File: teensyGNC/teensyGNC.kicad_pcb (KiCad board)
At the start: 4 copper layers, 57.5 x 129.5 mm, 32 parts, among them J1 5V_In_JST_XH, J10 TO_92_1_JST_PH, J11 TO_92_2_JST_PH, J12 TO_92_3_JST_PH, J13 TO_92_4_JST_PH, J2 ESC_1_PWM_1x03, J3 ESC_2_PWM_1x03, J4 Servo_1_PWM_1x03, J5 Servo_2_PWM_1x03, J6 7V4_In_XT30M, J7 I2C_INA_BM_JST_GH, J8 MTF_01P_JST_SH, J9 LC29H_Molex_4P, U1 LVL_Shift, U2 E28-2G4T20SX, U3 4754, U4 AP2112K-3.3, U5 DPS310, U6 Teensy4.1

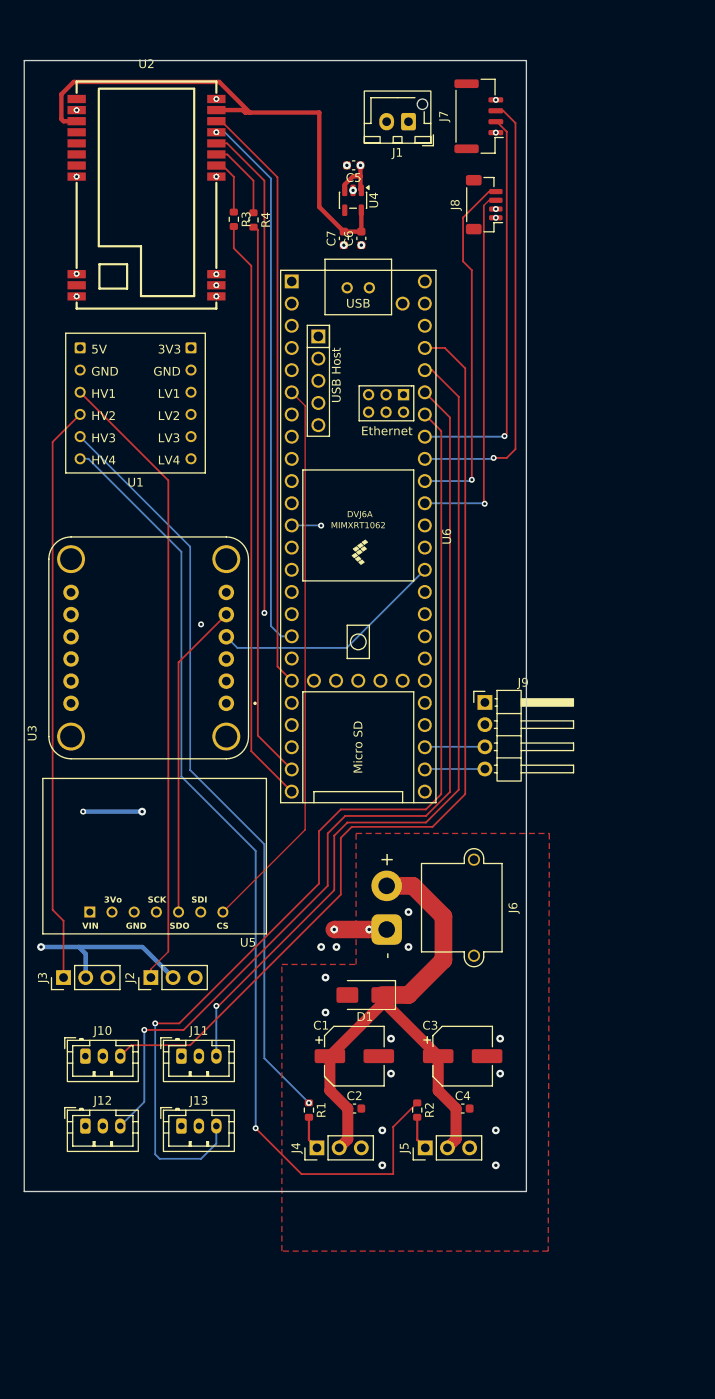
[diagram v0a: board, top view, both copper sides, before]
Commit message: More amendments
- Added mounting holes
- Removed splits in the ground plane by removing all in1.cu plane traces
- Added pull up/down resistors (check values)
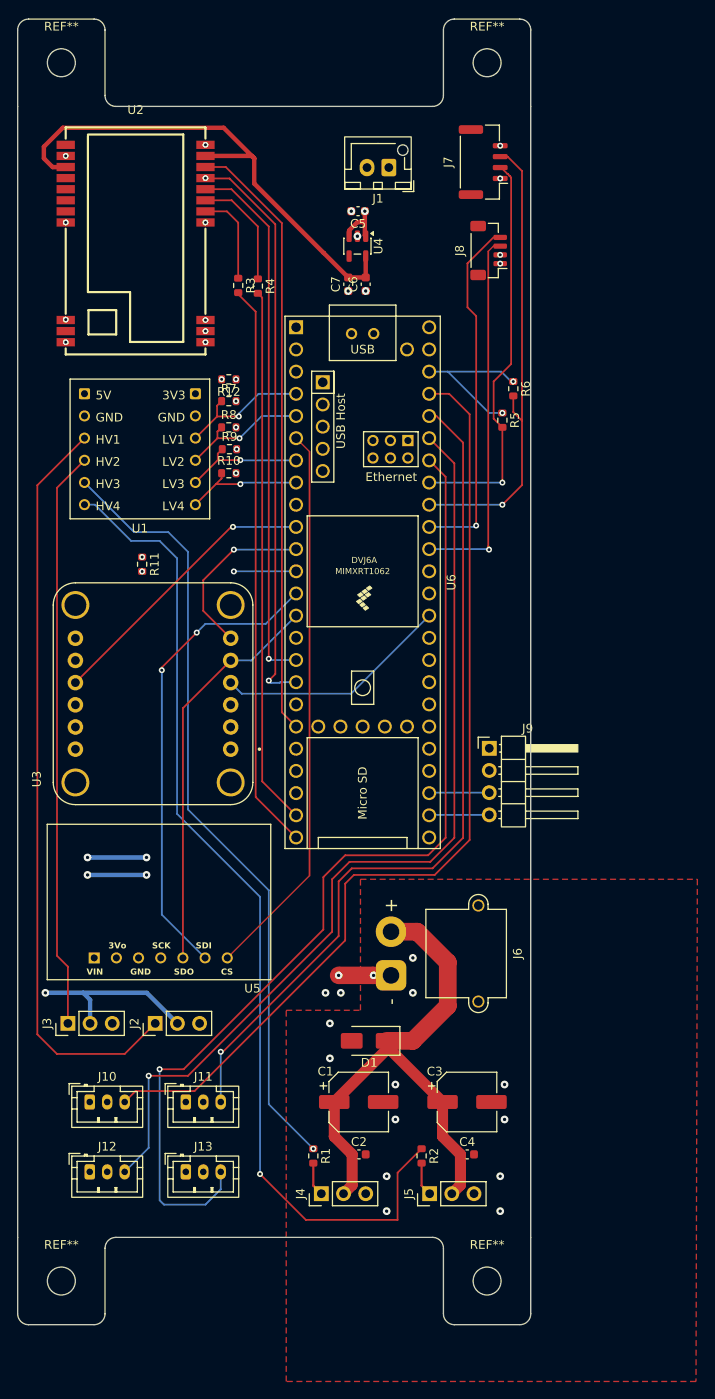
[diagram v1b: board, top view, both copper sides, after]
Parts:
- added R10: 10kΩ, Resistor_SMD:R_0603_1608Metric, F.Cu at (95.4, 78.8)
- added R11: 10kΩ, Resistor_SMD:R_0603_1608Metric, F.Cu at (85.5, 89.2)
- added R12: 10kΩ, Resistor_SMD:R_0603_1608Metric, F.Cu at (95.4, 68.0)
- added R5: 2.2kΩ, Resistor_SMD:R_0603_1608Metric, F.Cu at (126.8, 72.7)
- added R6: 2.2kΩ, Resistor_SMD:R_0603_1608Metric, F.Cu at (128.0, 69.1)
- added R7: 10kΩ, Resistor_SMD:R_0603_1608Metric, F.Cu at (95.4, 70.5)
- added R8: 10kΩ, Resistor_SMD:R_0603_1608Metric, F.Cu at (95.4, 73.5)
- added R9: 10kΩ, Resistor_SMD:R_0603_1608Metric, F.Cu at (95.5, 76.0)
- added REF**: MountingHole_3.2mm_M3, MountingHole:MountingHole_3.2mm_M3, F.Cu at (125.0, 31.8)
- added REF**: MountingHole_3.2mm_M3, MountingHole:MountingHole_3.2mm_M3, F.Cu at (125.0, 171.2)
- added REF**: MountingHole_3.2mm_M3, MountingHole:MountingHole_3.2mm_M3, F.Cu at (76.2, 31.8)
- added REF**: MountingHole_3.2mm_M3, MountingHole:MountingHole_3.2mm_M3, F.Cu at (76.2, 171.2)
- moved R3 7.59 mm to (96.5, 57.2)
- moved R4 7.59 mm to (98.8, 57.3)
- moved J1 5.71 mm to (113.8, 43.8)
- moved U2 5.40 mm to (84.8, 52.5)
- moved C1 5.27 mm to (110.3, 150.8)
- moved C2 5.27 mm to (110.3, 156.8)
- moved C3 5.27 mm to (122.7, 150.8)
- moved C4 5.27 mm to (122.7, 156.8)
- moved C5 5.27 mm to (110.2, 48.8)
- moved C6 5.27 mm to (111.1, 57.1)
- moved C7 5.27 mm to (109.1, 57.1)
- moved D1 5.27 mm to (111.5, 143.8)
- moved J10 5.27 mm to (79.5, 150.8)
- moved J11 5.27 mm to (90.5, 150.8)
- moved J12 5.27 mm to (79.5, 158.8)
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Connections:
- R3 pad 1: Net-(U2-M0) -> GND
- R3 pad 2: Net-(U6-32_OUT1B) -> Net-(U2-M0)
- R4 pad 1: Net-(U2-M1) -> GND
- R4 pad 2: Net-(U6-31_CTX3) -> Net-(U2-M1)
- U6 pad 2: /SPI.CS_BNO -> unconnected-(U6-0_RX1_CRX2_CS1-Pad2)
- U6 pad 23: Net-(U6-31_CTX3) -> Net-(U2-M1)
- U6 pad 24: Net-(U6-32_OUT1B) -> Net-(U2-M0)
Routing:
- net Net-(U2-M0): track 7.15 -> 76.4 mm
- net Net-(U6-32_OUT1B): track 67.5 -> 0.00 mm
- net Net-(U2-M1): track 9.74 -> 75.4 mm
- net Net-(U6-31_CTX3): track 64.0 -> 0.00 mm
- net /SPI.CS_BNO: track 70.8 -> 28.5 mm, vias 1 -> 2
- net +3V3: track 181.1 -> 209.4 mm, vias 2 -> 8
- net /SPI.DI: track 80.2 -> 64.5 mm, vias 1 -> 2
- net Net-(J2-Pin_1): track 72.0 -> 86.4 mm
- net /SPI.CS_DPS: track 64.0 -> 73.7 mm, vias 0 -> 1
- net /SPI.INT: track 13.3 -> 20.1 mm, vias 0 -> 1
- net +5V: track 237.1 -> 243.5 mm
- net Net-(U2-TXD): track 63.1 -> 66.6 mm, vias 1 -> 2
- net Net-(J7-Pin_3): track 51.0 -> 54.0 mm
- net Net-(U2-AUX): track 68.0 -> 70.3 mm
- net Net-(R1-Pad1): track 87.1 -> 89.4 mm
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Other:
- board size 57.5 x 129.5 mm -> 58.8 x 149.5 mm

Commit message: Moved LC29H onboard and to the top of the board
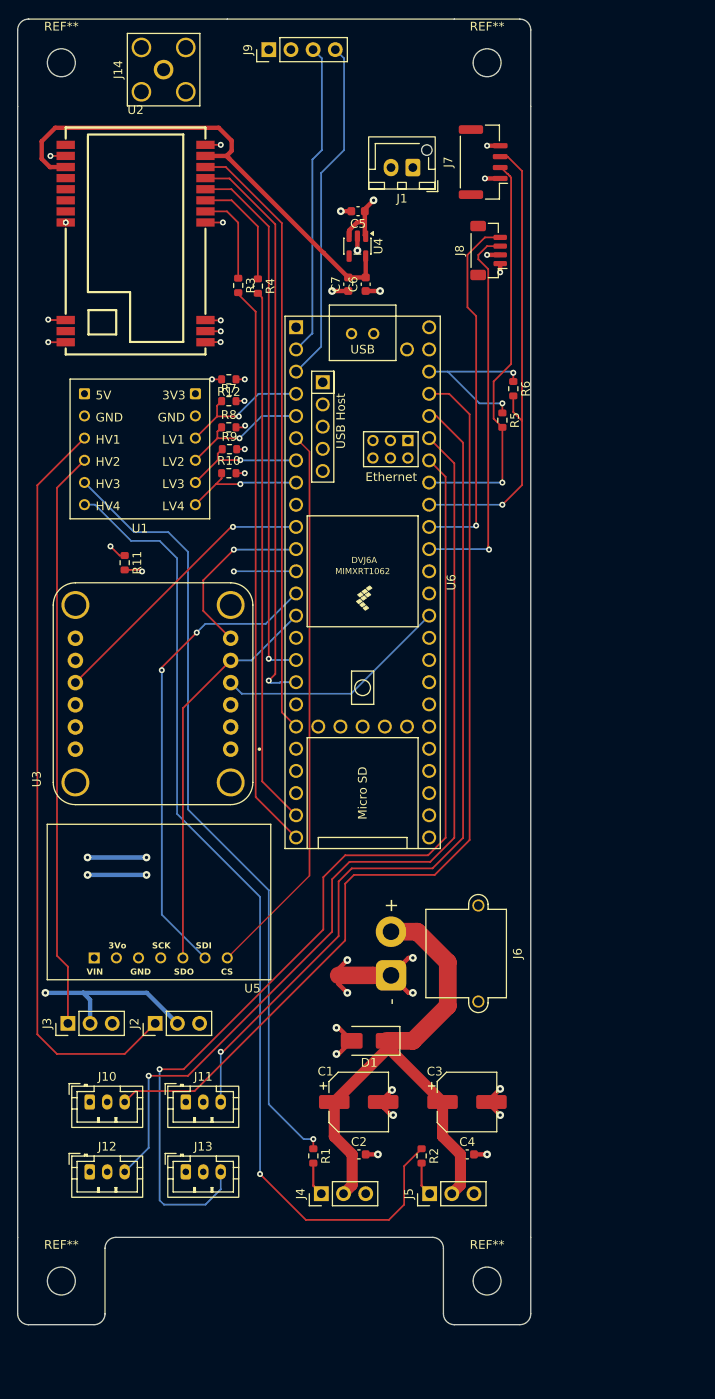
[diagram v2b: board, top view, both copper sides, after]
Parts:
- added J14: Conn_Coaxial, Connector_Coaxial:SMA_Amphenol_132203-12_Horizontal, F.Cu at (88.0, 32.5)
- J9: value LC29H_Molex_4P -> LC29H_1x04; footprint Connector_PinHeader_2.54mm:PinHeader_1x04_P2.54mm_Horizontal -> Connector_PinHeader_2.54mm:PinHeader_1x04_P2.54mm_Vertical
- moved J9 83.9 mm to (100.0, 30.2), turned to 90 degrees
- moved J1 2.75 mm to (116.5, 43.8)
- moved R11 2.01 mm to (83.5, 89.0)
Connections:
- U6 pad 2: unconnected-(U6-0_RX1_CRX2_CS1-Pad2) -> Net-(J9-Pin_3)
- U6 pad 26: Net-(J9-Pin_4) -> unconnected-(U6-34_RX8-Pad26)
- U6 pad 27: Net-(J9-Pin_3) -> unconnected-(U6-35_TX8-Pad27)
- U6 pad 3: unconnected-(U6-1_TX1_CTX2_MISO1-Pad3) -> Net-(J9-Pin_4)
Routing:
- net Net-(J9-Pin_4): track 6.97 -> 39.6 mm
- net GND: track 0.00 -> 32.2 mm, vias 22 -> 21
- net +5V: track 243.5 -> 211.6 mm
- net Net-(J9-Pin_3): track 6.97 -> 36.0 mm
- net PGND: track 0.00 -> 22.1 mm, vias 13 -> 10
- net /SPI.CS_BNO: track 28.5 -> 30.5 mm
- net Net-(U2-M2): track 59.0 -> 57.2 mm
- net Net-(J8-Pin_3): track 42.7 -> 44.0 mm
- net unconnected-(U2-ANT-Pad12): track 0.00 -> 0.71 mm
- net Net-(R1-Pad1): track 89.4 -> 90.1 mm
- net Net-(R2-Pad1): track 114.8 -> 114.2 mm
- net Net-(J8-Pin_4): track 40.9 -> 41.4 mm
- net /SPI.CS_DPS: track 73.7 -> 74.2 mm
- net Net-(U2-TXD): vias 2 -> 1
- removed copper zone on F.Cu, net PGND
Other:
- outline, holes or cut-outs redrawn
